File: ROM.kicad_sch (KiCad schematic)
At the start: 6 parts, among them U2 SST39SF040, U28 SST39SF040, U4 74LVC245AD

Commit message: work on FPGA
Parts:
- removed C16, C17, C18: 10u, stdpads:C_0805, symbol Device:C_Small
- removed U2: SST39SF040, stdpads:PLCC-32_SMDSocket, symbol GW_RAM:Flash-512Kx8-PLCC-32
- removed U28: SST39SF040, Package_DIP:DIP-32_W15.24mm_Socket_LongPads, symbol GW_RAM:Flash-512Kx8-PLCC-32
- removed U4: 74LVC245AD, stdpads:SOIC-20W_7.5mm, symbol GW_Logic:74245
- added C? (x2): 2u2, stdpads:C_0603, symbol Device:C_Small
- added U? (x2): W25Q64, stdpads:stdpads:SOIC-8_5.3mm, symbol GW_RAM:SPIFlash-SO-8
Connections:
- net +3V3: now also C?.1, C?.1, U?.8 (Vcc), U?.8 (Vcc)
- net GND: now also C?.2, C?.2, U?.4 (GND), U?.4 (GND)
- new net D2: U?.3 (~{WP}/IO2), U?.3 (~{WP}/IO2)
- new net D3: U?.7 (~{HLD}/IO3), U?.7 (~{HLD}/IO3)
- new net M0SI: U?.5 (DI/IO0), U?.5 (DI/IO0)
- new net M1SO: U?.2 (DO/IO1), U?.2 (DO/IO1)
- new net SCK0: U?.6 (CLK)
- new net SCK1: U?.6 (CLK)
- new net ~{CS}0: U?.1 (~{CS})
- new net ~{CS}1: U?.1 (~{CS})

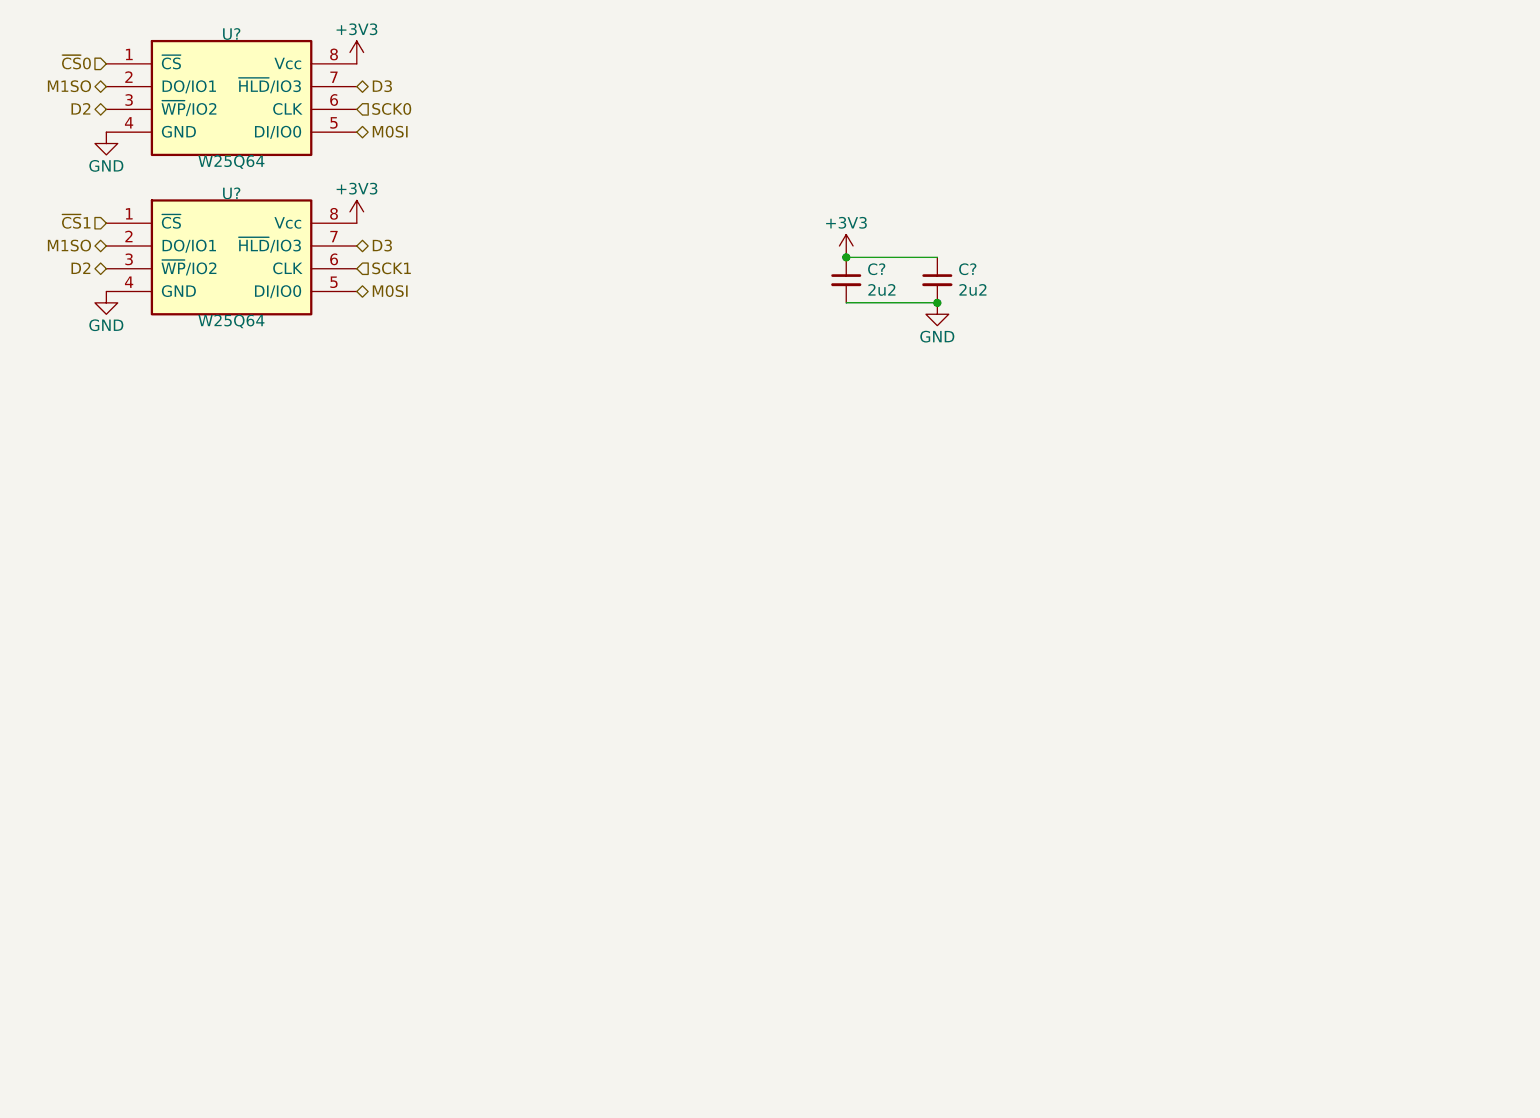
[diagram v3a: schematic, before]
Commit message: Revert "work on FPGA"
This reverts commit a96523e8d17974c7c48efc8a38ae046f7948cd49.
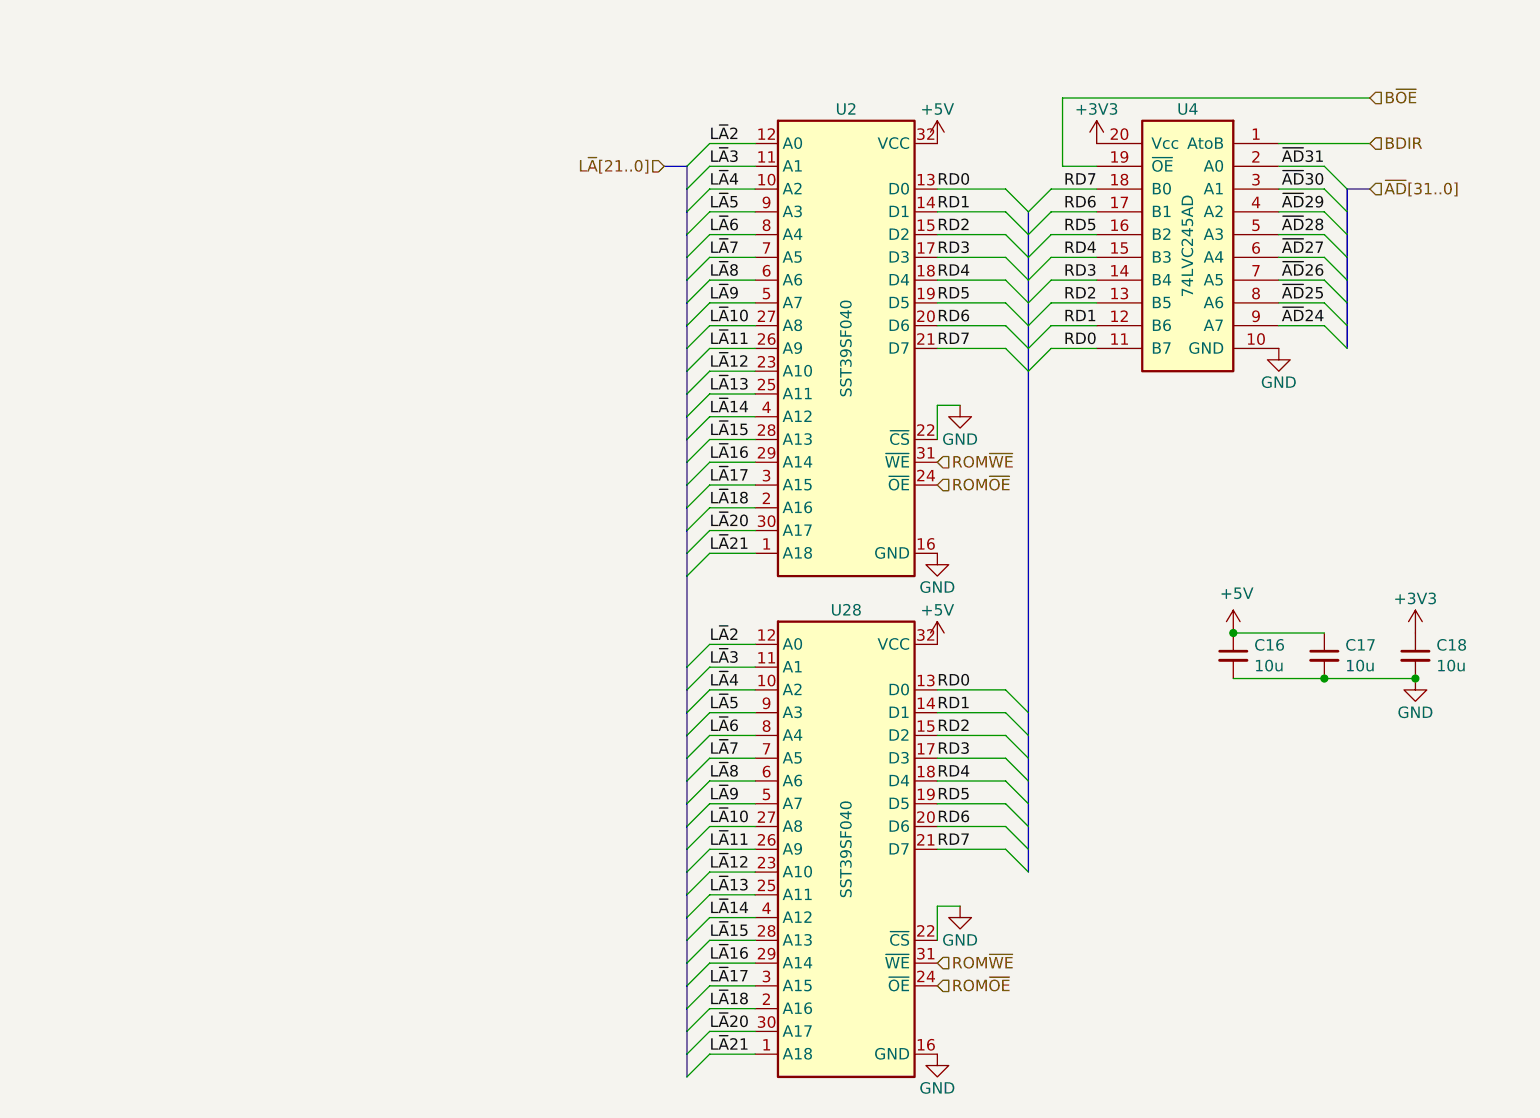
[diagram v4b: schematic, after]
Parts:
- removed C? (x2): 2u2, stdpads:C_0603, symbol Device:C_Small
- removed U? (x2): W25Q64, stdpads:stdpads:SOIC-8_5.3mm, symbol GW_RAM:SPIFlash-SO-8
- added C16, C17, C18: 10u, stdpads:C_0805, symbol Device:C_Small
- added U2: SST39SF040, stdpads:PLCC-32_SMDSocket, symbol GW_RAM:Flash-512Kx8-PLCC-32
- added U28: SST39SF040, Package_DIP:DIP-32_W15.24mm_Socket_LongPads, symbol GW_RAM:Flash-512Kx8-PLCC-32
- added U4: 74LVC245AD, stdpads:SOIC-20W_7.5mm, symbol GW_Logic:74245
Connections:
- net +3V3: now also C18.1, U4.20 (Vcc)
- net GND: now also C16.2, C17.2, C18.2, U2.16 (GND), U2.22 (~{CS}), U28.16 (GND), U28.22 (~{CS}), U4.10 (GND)
- new net +5V: C16.1, C17.1, U2.32 (VCC), U28.32 (VCC)
- new net BDIR: U4.1 (AtoB)
- new net B~{OE}: U4.19 (~{OE})
- new net L~{A}10: U2.27 (A8), U28.27 (A8)
- new net L~{A}11: U2.26 (A9), U28.26 (A9)
- new net L~{A}12: U2.23 (A10), U28.23 (A10)
- new net L~{A}13: U2.25 (A11), U28.25 (A11)
- new net L~{A}14: U2.4 (A12), U28.4 (A12)
- new net L~{A}15: U2.28 (A13), U28.28 (A13)
- new net L~{A}16: U2.29 (A14), U28.29 (A14)
- new net L~{A}17: U2.3 (A15), U28.3 (A15)
- new net L~{A}18: U2.2 (A16), U28.2 (A16)
- new net L~{A}2: U2.12 (A0), U28.12 (A0)
- new net L~{A}20: U2.30 (A17), U28.30 (A17)
- new net L~{A}21: U2.1 (A18), U28.1 (A18)
- new net L~{A}3: U2.11 (A1), U28.11 (A1)
- new net L~{A}4: U2.10 (A2), U28.10 (A2)
- new net L~{A}5: U2.9 (A3), U28.9 (A3)
- new net L~{A}6: U2.8 (A4), U28.8 (A4)
- new net L~{A}7: U2.7 (A5), U28.7 (A5)
- new net L~{A}8: U2.6 (A6), U28.6 (A6)
- new net L~{A}9: U2.5 (A7), U28.5 (A7)
- new net RD0: U2.13 (D0), U28.13 (D0), U4.11 (B7)
- new net RD1: U2.14 (D1), U28.14 (D1), U4.12 (B6)
- new net RD2: U2.15 (D2), U28.15 (D2), U4.13 (B5)
- new net RD3: U2.17 (D3), U28.17 (D3), U4.14 (B4)
- new net RD4: U2.18 (D4), U28.18 (D4), U4.15 (B3)
- new net RD5: U2.19 (D5), U28.19 (D5), U4.16 (B2)
- new net RD6: U2.20 (D6), U28.20 (D6), U4.17 (B1)
- new net RD7: U2.21 (D7), U28.21 (D7), U4.18 (B0)
- new net ROM~{OE}: U2.24 (~{OE}), U28.24 (~{OE})
- new net ROM~{WE}: U2.31 (~{WE}), U28.31 (~{WE})
- new net ~{AD}24: U4.9 (A7)
- new net ~{AD}25: U4.8 (A6)
- new net ~{AD}26: U4.7 (A5)
- new net ~{AD}27: U4.6 (A4)
- new net ~{AD}28: U4.5 (A3)
- new net ~{AD}29: U4.4 (A2)
- new net ~{AD}30: U4.3 (A1)
- new net ~{AD}31: U4.2 (A0)
